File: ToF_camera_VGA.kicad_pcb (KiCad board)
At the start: 4 copper layers, 48 x 49 mm, 57 parts, among them J1 Conn_01x22, J2 Conn_01x01, J3 Conn_01x04, J4 Conn_01x01, J5 Conn_01x04, J6 Conn_01x04, J8 Conn_01x02, SW1 SW_Push, U1 TPS82150, U2 MLX75027, U3 TPS82150, U4 TPS82150, U5 TPSM84624, U6 PCA9306, Y1 Crystal

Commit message: Updated BOM
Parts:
- C10, C14, C3: value 3.3n -> 430p, 1m
- C16: footprint Capacitors_SMD:CP_Elec_4x5.8 -> Capacitors_SMD:CP_Elec_5x5.8
- C9: value 10u -> 10u, 2.229 mOhm
- R1, R17, R2: value R -> 10k
- R4: value 124k -> 237k
- R7: value 124k -> 49.9k
- Y1: footprint Crystals:Crystal_SMD_2012-2pin_2.0x1.2mm -> Crystals:Crystal_SMD_5032-2pin_5.0x3.2mm
- moved Y1 2.74 mm to (107.8, 115.8), turned to 90 degrees
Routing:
- net GNDD: track 192.0 -> 199.1 mm, vias 65 -> 66
- net +1V2: track 36.4 -> 39.5 mm

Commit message: Minor updates, production read. Added Gerbers
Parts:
- added R18: R, Resistors_SMD:R_0805, F.Cu at (134.1, 108.1)
- moved R4 7.51 mm to (135.1, 105.5), turned to 270 degrees
- moved R3 2.47 mm to (128.3, 104.6)
- moved Y1 1.27 mm to (106.5, 115.7)
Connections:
- R4 pad 2: VDDA -> Net-(R18-Pad2)
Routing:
- net Net-(R3-Pad2): track 2.90 -> 10.2 mm, vias 0 -> 2
- net GNDA: track 103.9 -> 106.4 mm
- net Net-(R18-Pad2): track 0.00 -> 1.68 mm
- net Net-(U2-PadB3): track 6.50 -> 7.32 mm
- net GNDD: track 199.1 -> 198.3 mm
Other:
- board text added: "+12V"
- board text added: "GND"
- board text added: "LEDEN"
- board text added: "LEDFB"
- board text added: "LED_N"
- board text added: "LED_P"
- board text added: "RST"
- board text added: "TRIGGER"
- board text added: "linas rudalevicius 2019"
- board text removed: "FROM HERE COMES +12V"
- board text removed: "TOP and BOTTOM - CSI-2 Signals, inner layers - CSI-2 GND"

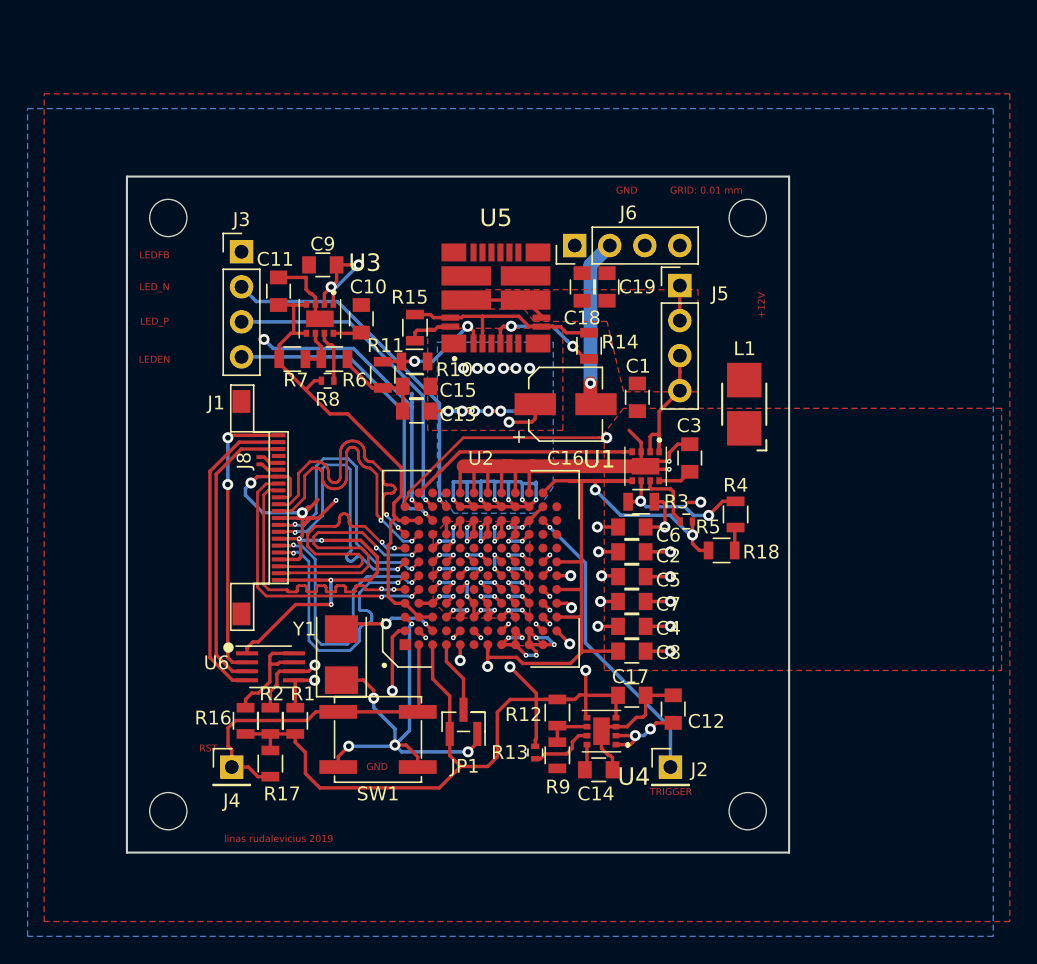
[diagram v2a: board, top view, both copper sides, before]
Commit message: Version 2 with fixed following issues: 1. clock source added 2. Flat cable connector should be ok 3. I2C level shifter should be ok 4. Power tree simplified, 12 V needed only for VDDMIX, others are generated from 3.3 V on flat cable
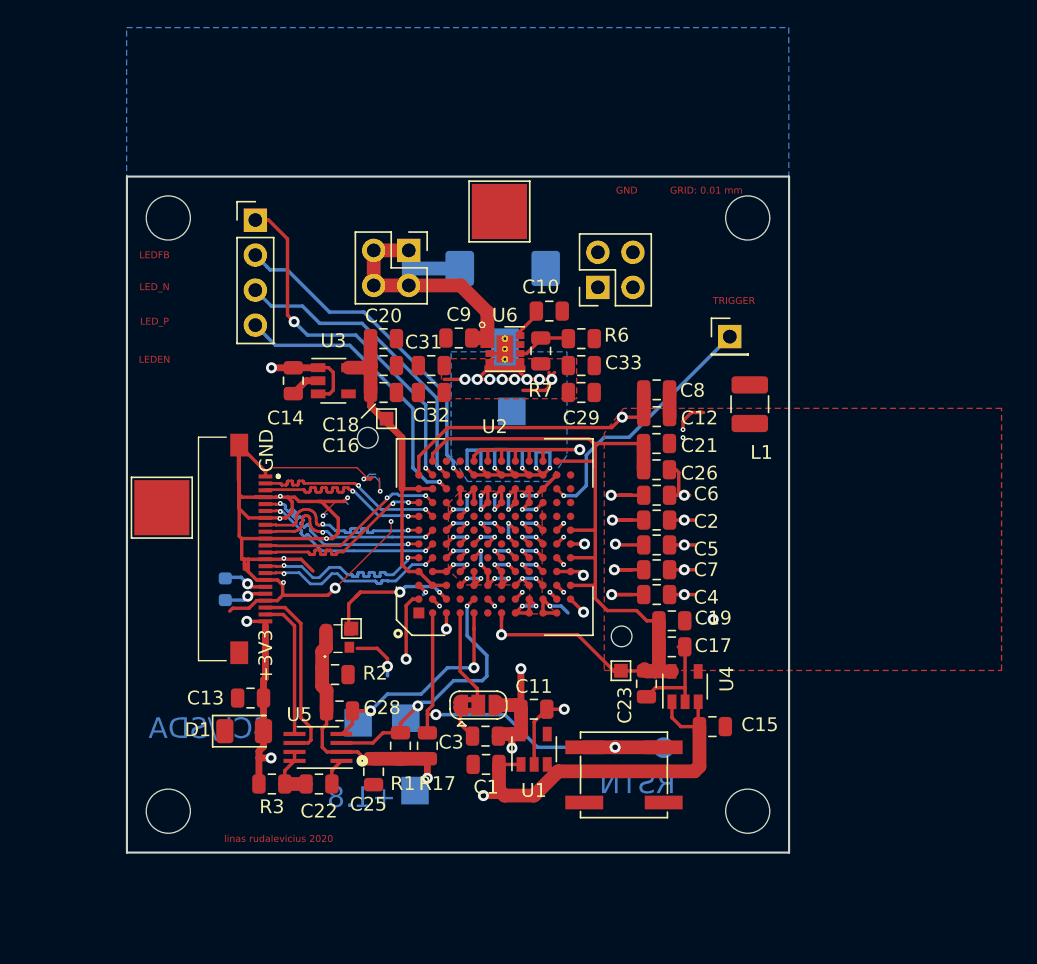
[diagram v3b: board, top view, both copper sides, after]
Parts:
- removed J8: Conn_01x02, Resistors_SMD:R_0201_NoSilk
- removed JP1: SolderJumper_3_Open, Pin_Headers:Pin_Header_Straight_1x03_Pitch1.00mm_SMD_Pin1Right
- removed R10, R11: 10k, Resistors_SMD:R_0805
- removed R12: 124k, Resistors_SMD:R_0805
- removed R13, R5, R8: 100k, Resistors_SMD:R_0402
- removed R14: 4.12k, Resistors_SMD:R_0805
- removed R15: 110k, Resistors_SMD:R_0805
- removed R16: 200k, Resistors_SMD:R_0805
- removed R18: R, Resistors_SMD:R_0805
- removed R4: 237k, Resistors_SMD:R_0805
- removed R9: 100k, Resistors_SMD:R_0805
- added C20: 100n, Capacitor_SMD:C_0805_2012Metric, F.Cu at (109.6, 92.8)
- added C21: 10u, Capacitor_SMD:C_0805_2012Metric, F.Cu at (129.4, 100.3)
- added C22: 100n, Capacitor_SMD:C_0805_2012Metric, F.Cu at (104.9, 125.0)
- added C23: 100n, Capacitor_SMD:C_0805_2012Metric, F.Cu at (128.7, 117.8)
- added C25: 100n, Capacitor_SMD:C_0805_2012Metric, F.Cu at (108.9, 124.1)
- added C26: 100n, Capacitor_SMD:C_0805_2012Metric, F.Cu at (129.4, 102.2)
- added C28: 1u, Capacitor_SMD:C_0805_2012Metric, F.Cu at (106.1, 117.1)
- added C29: 10u, Capacitor_SMD:C_0805_2012Metric, F.Cu at (123.9, 96.7)
- added C31: 10u, Capacitor_SMD:C_0805_2012Metric, F.Cu at (113.1, 94.7)
- added C32: 100n, Capacitor_SMD:C_0805_2012Metric, F.Cu at (113.1, 96.7)
- added C33: 100n, Capacitor_SMD:C_0805_2012Metric, F.Cu at (123.9, 94.7)
- added CP27: 68u, Capacitor_Tantalum_SMD:CP_EIA-7343-30_AVX-N, B.Cu at (118.2, 87.7)
- added D1: LED, LED_SMD:LED_1206_3216Metric, F.Cu at (99.5, 121.2)
- added H1: MountingHole, myFootprints:MountingHole_1.5mm, F.Cu at (108.5, 99.9)
- added H2: MountingHole, myFootprints:MountingHole_1.5mm, F.Cu at (126.9, 114.3)
- added J10: Conn_01x01, TestPoint:TestPoint_Pad_2.0x2.0mm, B.Cu at (111.9, 125.5)
- added J11: Conn_01x01, TestPoint:TestPoint_Pad_1.0x1.0mm, F.Cu at (109.8, 98.5)
- added J12: Conn_01x01, TestPoint:TestPoint_Pad_2.0x2.0mm, B.Cu at (111.2, 120.3)
- added J13: Conn_01x01, TestPoint:TestPoint_Pad_1.0x1.0mm, F.Cu at (126.8, 116.8)
- added J14: Conn_01x01, TestPoint:TestPoint_Pad_2.0x2.0mm, B.Cu at (107.8, 120.6)
- added J15: Conn_01x01, TestPoint:TestPoint_Pad_1.0x1.0mm, F.Cu at (107.3, 113.8)
- added J16: Conn_01x01, TestPoint:TestPoint_Pad_2.0x2.0mm, B.Cu at (118.9, 98.0)
- added J17: Conn_01x01, TestPoint:TestPoint_Pad_4.0x4.0mm, F.Cu at (118.0, 83.5)
- added J18: Conn_01x01, TestPoint:TestPoint_Pad_4.0x4.0mm, F.Cu at (93.5, 105.0)
- added J7: Conn_01x02, Resistor_SMD:R_0603_1608Metric, B.Cu at (98.1, 110.9)
- added J9: Conn_01x03, Jumper:SolderJumper-3_P1.3mm_Bridged2Bar12_RoundedPad1.0x1.5mm, F.Cu at (116.5, 119.3)
- C1: value 10u -> 1u; footprint Capacitors_SMD:C_0805 -> Capacitor_SMD:C_0805_2012Metric
- C10: value 430p, 1m -> 430p; footprint Capacitors_SMD:C_0805 -> Capacitor_SMD:C_0805_2012Metric
- C11: value 22u -> 100n; footprint Capacitors_SMD:C_0805 -> Capacitor_SMD:C_0805_2012Metric
- C12: value 10u -> 100n; footprint Capacitors_SMD:C_0805 -> Capacitor_SMD:C_0805_2012Metric
- C13: value 100u -> 10u; footprint Capacitors_SMD:C_0805 -> Capacitor_SMD:C_0805_2012Metric
- C14, C3: value 430p, 1m -> 1u; footprint Capacitors_SMD:C_0805 -> Capacitor_SMD:C_0805_2012Metric
- C15: value 100u -> 1u; footprint Capacitors_SMD:C_0805 -> Capacitor_SMD:C_0805_2012Metric
- C16: value 220u -> 1u; footprint Capacitors_SMD:CP_Elec_5x5.8 -> Capacitor_SMD:C_0805_2012Metric
- C17: value 22u -> 1u; footprint Capacitors_SMD:C_0805 -> Capacitor_SMD:C_0805_2012Metric
- C18, C19, C2, C4, C5, C6, C7: footprint Capacitors_SMD:C_0805 -> Capacitor_SMD:C_0805_2012Metric
- C8: value 22u -> 10u; footprint Capacitors_SMD:C_0805 -> Capacitor_SMD:C_0805_2012Metric
- C9: value 10u, 2.229 mOhm -> 10u; footprint Capacitors_SMD:C_0805 -> Capacitor_SMD:C_0805_2012Metric
- J1: value Conn_01x22 -> 54548-2271_connector_RPi_zero; footprint myFootprints:FPC_22 -> myFootprints:545482271_RPi_Zero_connector
- J2: footprint Pin_Headers:Pin_Header_Straight_1x01_Pitch2.54mm -> Connector_PinHeader_2.54mm:PinHeader_1x01_P2.54mm_Vertical
- J3: footprint Pin_Headers:Pin_Header_Straight_1x04_Pitch2.54mm -> Connector_PinHeader_2.54mm:PinHeader_1x04_P2.54mm_Vertical
- J4: footprint Pin_Headers:Pin_Header_Straight_1x01_Pitch2.54mm -> TestPoint:TestPoint_Pad_D1.5mm; moved to B.Cu
- J5, J6: footprint Pin_Headers:Pin_Header_Straight_1x04_Pitch2.54mm -> Connector_PinHeader_2.54mm:PinHeader_2x02_P2.54mm_Vertical
- L1: footprint Inductors:Inductor_1212 -> Inductor_SMD:L_1210_3225Metric
- MK1, MK2, MK3, MK4: footprint Mounting_Holes:MountingHole_2.7mm -> MountingHole:MountingHole_3.2mm_M3
- R1, R2: value 10k -> 1k5; footprint Resistors_SMD:R_0805 -> Resistor_SMD:R_0805_2012Metric
- R17, R6, R7: footprint Resistors_SMD:R_0805 -> Resistor_SMD:R_0805_2012Metric
- R3: value 100k -> 200k; footprint Resistors_SMD:R_0805 -> Resistor_SMD:R_0805_2012Metric
- SW1: footprint Buttons_Switches_SMD:SW_SPST_EVPBF -> Button_Switch_SMD:SW_SPST_EVPBF
- U1: value TPS82150 -> LP5907MFX-1.8; footprint myFootprints:TPS82130 -> Package_TO_SOT_SMD:SOT-23-5
- U2: footprint myFootprints:MLX75027 -> myFootprints:MLX75027_NSMD
- U3: value TPS82150 -> LP5907MFX-1.2; footprint myFootprints:TPS82130 -> Package_TO_SOT_SMD:SOT-23-5
- U4: value TPS82150 -> LP5907MFX-2.8; footprint myFootprints:TPS82130 -> Package_TO_SOT_SMD:SOT-23-5
- U5: value TPSM84624 -> PCA9306; footprint myFootprints:TPSM84624 -> Package_SO:SSOP-8_2.95x2.8mm_P0.65mm
- U6: value PCA9306 -> TPS82130; footprint Housings_SSOP:SSOP-8_2.95x2.8mm_Pitch0.65mm -> Package_LGA:Texas_SIL0008D_MicroSiP-8-1EP_2.8x3mm_P0.65mm_EP1.1x1.9mm_ThermalVias
- Y1: value Crystal -> DSC6011JI1A-008.0000_clock_source; footprint Crystals:Crystal_SMD_5032-2pin_5.0x3.2mm -> myFootprints:DSC6011JI1A0080000_clock_source
- moved C14 35.9 mm to (103.1, 95.8), turned to 270 degrees
- moved C11 35.5 mm to (120.5, 119.6), turned to 0 degrees
- moved U5 35.0 mm to (104.8, 122.4), turned to 180 degrees
- moved R3 33.7 mm to (101.5, 125.0)
- moved C15 32.7 mm to (133.4, 120.9), turned to 0 degrees
- moved J2 31.5 mm to (134.7, 92.6)
- moved J4 31.3 mm to (129.9, 122.4), turned to 90 degrees
- moved C1 28.8 mm to (117.0, 123.6), turned to 180 degrees
- moved U6 28.6 mm to (118.4, 93.5)
- moved C3 25.0 mm to (117.0, 121.6), turned to 180 degrees
- moved C19 24.7 mm to (130.5, 113.2), turned to 0 degrees
- moved C13 24.0 mm to (100.0, 118.8)
- moved U1 22.0 mm to (120.5, 122.5), turned to 90 degrees
- moved C12 21.2 mm to (129.4, 98.4), turned to 0 degrees
- moved J5 19.8 mm to (111.4, 86.3), turned to 270 degrees
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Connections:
- C1 pad 1: +12V -> /3V3_Pi
- C1 pad 2: GNDA -> GNDD
- C11 pad 1: VDD -> +1V8
- C12 pad 1: +12V -> +1V8
- C13 pad 1: +1V2 -> /3V3_Pi
- C14 pad 1: Net-(C14-Pad1) -> /3V3_Pi
- C15 pad 1: +1V2 -> /3V3_Pi
- C16 pad 1: +1V2 -> VDD
- C17 pad 1: +1V8 -> VDDA
- C17 pad 2: GNDD -> GNDA
- C18 pad 1: +12V -> VDD
- C19 pad 1: +12V -> VDDA
- C19 pad 2: GNDD -> GNDA
- C3 pad 1: Net-(C3-Pad1) -> +1V8
- C3 pad 2: GNDA -> GNDD
- C8 pad 1: VDDA -> +1V8
- C8 pad 2: GNDA -> GNDD
- J1 pad 1: /3V3_Pi -> GNDD
- J1 pad 11: /D3+ -> /D3-
- J1 pad 12: /D3- -> /D3+
- J1 pad 14: /CLK+ -> /D4-
- J1 pad 15: /CLK- -> /D4+
- J1 pad 17: /D2+ -> Net-(J1-Pad17)
- J1 pad 18: /D2- -> Net-(J1-Pad18)
- J1 pad 2: /SDA_Pi -> /D1-
- J1 pad 20: /D1+ -> /SCL_Pi
- J1 pad 21: /D1- -> /SDA_Pi
- J1 pad 22: GNDD -> /3V3_Pi
- J1 pad 3: /SCL_Pi -> /D1+
- J1 pad 4: (no net) -> GNDD
- J1 pad 5: Net-(J1-Pad5) -> /D2-
- J1 pad 6: Net-(J1-Pad6) -> /D2+
- J1 pad 8: /D4+ -> /CLK-
- J1 pad 9: /D4- -> /CLK+
- L1 pad 1: GNDA -> GNDD
- L1 pad 2: GNDD -> GNDA
- MK1 pad 1: (no net) -> GNDD
- MK2 pad 1: (no net) -> GNDD
- MK3 pad 1: (no net) -> GNDD
- MK4 pad 1: (no net) -> GNDD
- R1 pad 2: Net-(R1-Pad2) -> /SCL
- R2 pad 2: Net-(R2-Pad2) -> /SDA
- R3 pad 1: GNDA -> Net-(C22-Pad1)
- R3 pad 2: Net-(R3-Pad2) -> /3V3_Pi
- R7 pad 2: VDD -> +1V2
- U1 pad 1: +12V -> /3V3_Pi
- U1 pad 2: +12V -> GNDD
- U1 pad 3: GNDA -> /3V3_Pi
- U1 pad 4: VDDA -> (no net)
- U1 pad 5: VDDA -> +1V8
- U2 pad A5: Net-(R1-Pad2) -> /SDA
- U2 pad A6: (no net) -> Net-(U2-PadA6)
- U2 pad B3: Net-(U2-PadB3) -> /CLK
- U2 pad B4: (no net) -> Net-(U2-PadB4)
- U2 pad B5: Net-(R2-Pad2) -> /SCL
- U2 pad B7: (no net) -> Net-(U2-PadB7)
- U2 pad H11: (no net) -> Net-(U2-PadH11)
- U2 pad H12: (no net) -> Net-(U2-PadH12)
- U2 pad J11: (no net) -> Net-(U2-PadJ11)
- U2 pad J12: (no net) -> Net-(U2-PadJ12)
- U2 pad K12: (no net) -> Net-(U2-PadK12)
- U2 pad L12: (no net) -> Net-(U2-PadL12)
- U2 pad M3: (no net) -> Net-(U2-PadM3)
- U2 pad M4: (no net) -> Net-(U2-PadM4)
- U3 pad 1: +12V -> /3V3_Pi
- U3 pad 2: +12V -> GNDD
- U3 pad 3: GNDD -> /3V3_Pi
- U3 pad 4: VDD -> (no net)
- U4 pad 1: +12V -> /3V3_Pi
- U4 pad 2: +12V -> GNDA
- U4 pad 3: GNDD -> /3V3_Pi
- U4 pad 4: +1V8 -> (no net)
- U4 pad 5: +1V8 -> VDDA
- U5 pad 1: +1V2 -> GNDD
- U5 pad 2: Net-(R10-Pad1) -> +1V8
- U5 pad 3: Net-(R14-Pad2) -> /SCL
- U5 pad 4: (no net) -> /SDA
- U5 pad 5: Net-(R14-Pad1) -> /SDA_Pi
- U5 pad 6: (no net) -> /SCL_Pi
- U5 pad 7: (no net) -> Net-(C22-Pad1)
- U5 pad 8: +1V2 -> Net-(C22-Pad1)
- U6 pad 1: GNDD -> +12V
- U6 pad 2: /3V3_Pi -> +12V
- U6 pad 3: /SCL_Pi -> GNDD
- U6 pad 4: /SDA_Pi -> +1V2
- U6 pad 5: Net-(R1-Pad2) -> +1V2
- U6 pad 6: Net-(R2-Pad2) -> Net-(R6-Pad2)
- U6 pad 7: Net-(R16-Pad2) -> Net-(U6-Pad7)
- U6 pad 8: Net-(R16-Pad2) -> Net-(C10-Pad1)
- Y1 pad 1: GNDD -> +1V8
- Y1 pad 2: Net-(U2-PadB3) -> GNDD
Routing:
- net /3V3_Pi: track 21.2 -> 94.7 mm, vias 2 -> 4
- net /SCL: track 0.00 -> 19.3 mm, vias 0 -> 2
- net Net-(R2-Pad2): track 17.2 -> 0.00 mm, vias 2 -> 0
- net GNDA: track 106.4 -> 89.2 mm, vias 14 -> 13
- net /SDA: track 0.00 -> 16.8 mm, vias 0 -> 2
- net Net-(R1-Pad2): track 15.8 -> 0.00 mm, vias 2 -> 0
- net Net-(R14-Pad2): track 15.2 -> 0.00 mm
- net /SDA_Pi: track 22.7 -> 10.3 mm
- net VDD: track 36.6 -> 25.1 mm
- net +12V: track 34.1 -> 23.3 mm, vias 4 -> 0
- net /CLK: track 0.00 -> 10.5 mm, vias 0 -> 2
- net Net-(R3-Pad2): track 10.2 -> 0.00 mm, vias 2 -> 0
- net GNDD: track 198.3 -> 188.6 mm, vias 66 -> 64
- net Net-(R10-Pad1): track 8.73 -> 0.00 mm, vias 2 -> 0
- net Net-(R14-Pad1): track 8.54 -> 0.00 mm, vias 2 -> 0
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- removed copper zone on F.Cu, net +12V
- removed copper zone on In2.Cu, net +12V
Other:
- board text added: "+1.8"
- board text added: "+3V3"
- board text added: "RSTN"
- board text added: "SCL/SDA"
- board text added: "linas rudalevicius 2020"
- board text removed: "+12V"
- board text removed: "RST"
- board text removed: "linas rudalevicius 2019"

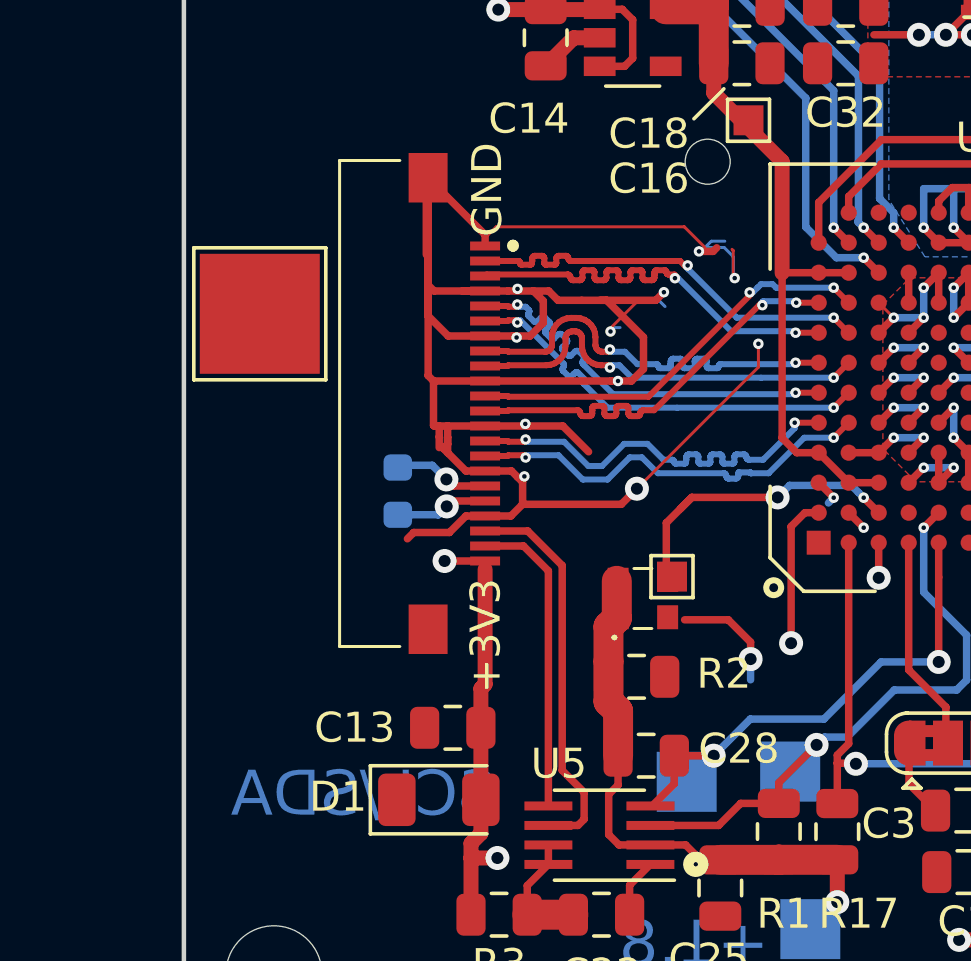
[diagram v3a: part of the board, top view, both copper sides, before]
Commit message: Flat cable connector fixed. The right part is Molex 5034802200
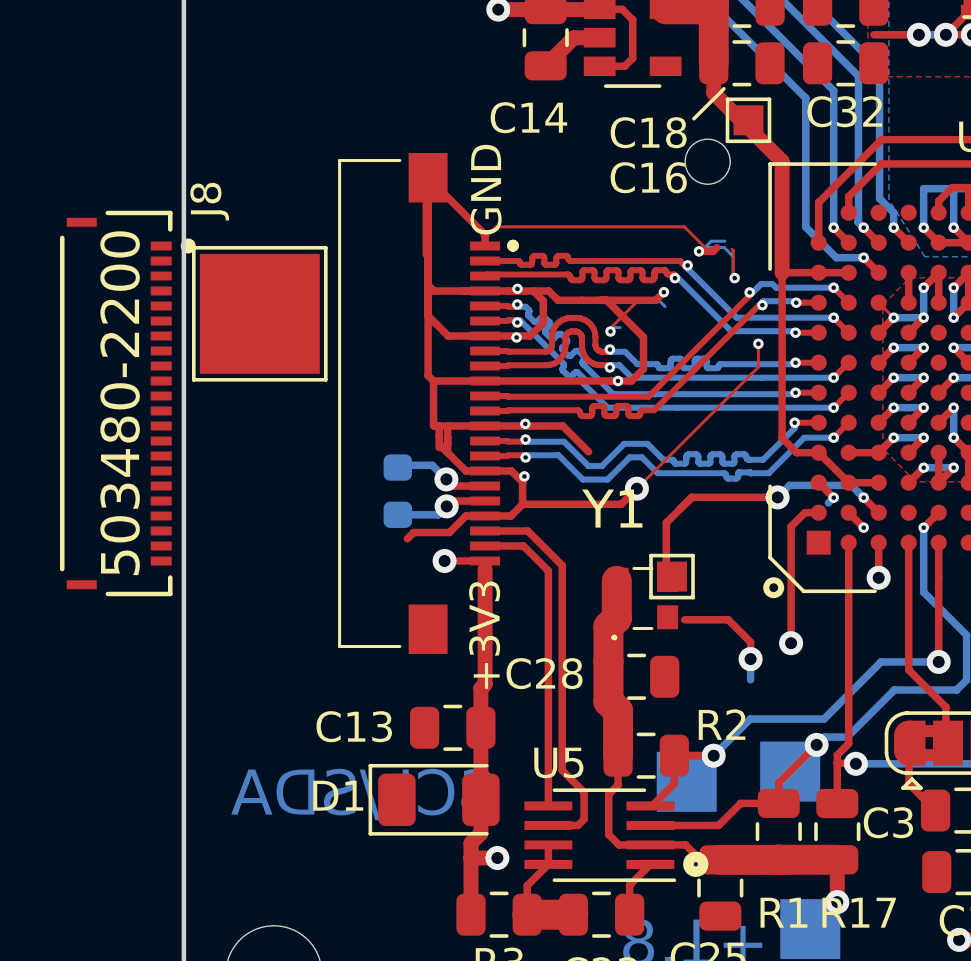
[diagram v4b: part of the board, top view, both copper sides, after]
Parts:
- added J8: 503480-2200, myFootprints:Molex-503480-2200, F.Cu at (88.9, 108.0)

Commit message: Picture added
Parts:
- removed J1: 54548-2271_connector_RPi_zero, myFootprints:545482271_RPi_Zero_connector
- moved J8 10.8 mm to (99.7, 108.0)
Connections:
- J7 pad 1: Net-(J1-Pad18) -> Net-(J7-Pad1)
- J7 pad 2: Net-(J1-Pad17) -> Net-(J7-Pad2)
- J8 pad 17: (no net) -> Net-(J7-Pad2)
- J8 pad 18: (no net) -> Net-(J7-Pad1)
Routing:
- net Net-(J7-Pad2): track 0.00 -> 3.23 mm, vias 0 -> 1
- net Net-(J1-Pad17): track 3.23 -> 0.00 mm, vias 1 -> 0
- net Net-(J7-Pad1): track 0.00 -> 3.10 mm, vias 0 -> 1
- net Net-(J1-Pad18): track 3.10 -> 0.00 mm, vias 1 -> 0
